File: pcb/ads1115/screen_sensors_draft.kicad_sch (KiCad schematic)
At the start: 12 parts, among them J1 WAVESHARE_I2C, J2 BOILER_PROBE, J3 XDB401_ANALOG, U1 ADS1115IDGSR, U2 SHT40-AD1B

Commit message: Screen Sensors PCB
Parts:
- J1: Note Pin 1 VCC/3V3, 2 GND, 3 SDA, 4 SCL; matches Waveshare order -> Pin 1 VCC/3V3, 2 GND, 3 SCL, 4 SDA; cross SDA/SCL in Wavesh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
- renumbered C4 to C3, C5 to C4, C6 to C5
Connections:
- net SCL: now also J1.3 (Pin_3); no longer J1.4 (Pin_4)
- net SDA: now also J1.4 (Pin_4); no longer J1.3 (Pin_3)
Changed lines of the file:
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@@
 (label "GND" (at 38.1 50.8 180) (effects (font (size 1.0 1.0))))
 (wire (pts (xy 43.18 53.34) (xy 38.1 53.34)) (stroke (width 0) (type default)))
-(label "SDA" (at 38.1 53.34 180) (effects (font (size 1.0 1.0))))
+(label "SCL" (at 38.1 53.34 180) (effects (font (size 1.0 1.0))))
 (wire (pts (xy 43.18 55.88) (xy 38.1 55.88)) (stroke (width 0) (type default)))
-(label "SCL" (at 38.1 55.88 180) (effects (font (size 1.0 1.0))))
+(label "SDA" (at 38.1 55.88 180) (effects (font (size 1.0 1.0))))
 (symbol (lib_id "Connector_Generic:Conn_01x04") (at 48.26 50.8 0) (unit 1) (in_bom yes) (on_board yes) (dnp no)
 (property "Reference" "J1" (at 48.26 45.72 0) (effects (font (size 1.0 1.0)) ))
@@
 (property "MPN" "B4B-XH-A(LF)(SN)" (at 48.26 58.8 0) (effects (font (size 1.0 1.0)) (hide yes)))
 (property "LCSC" "C144395" (at 48.26 58.8 0) (effects (font (size 1.0 1.0)) (hide yes)))
-(property "Note" "Pin 1 VCC/3V3, 2 GND, 3 SDA, 4 SCL; matches Waveshare order" (at 48.26 58.8 0) (effects (font (size 1.0 1.0)) (hide yes)))
+(property "Note" "Pin 1 VCC/3V3, 2 GND, 3 SCL, 4 SDA; cross SDA/SCL in Waveshare cable" (at 48.26 58.8 0) (effects (font (size 1.0 1.0)) (hide yes)))
 (pin "1")
 (pin "2")
@@
 (label "GND" (at 238.76 125.73 0) (effects (font (size 1.0 1.0))))
 (symbol (lib_id "Device:C") (at 233.68 116.84 0) (unit 1) (in_bom yes) (on_board yes) (dnp no)
-(property "Reference" "C4" (at 234.315 114.3 0) (effects (font (size 1.0 1.0)) ))
+(property "Reference" "C3" (at 234.315 114.3 0) (effects (font (size 1.0 1.0)) ))
 (property "Value" "100nF" (at 234.315 119.38000000000001 0) (effects (font (size 1.0 1.0)) ))
 (property "Footprint" "Capacitor_SMD:C_0603_1608Metric" (at 234.64520000000002 120.65 0) (effects (font (size 1.0 1.0)) (hide yes)))
@@
 (pin "1")
 (pin "2")
-(instances (project "screen_sensors_draft" (path "/b733619e-0a21-4de7-9d63-5b29c9c92157" (reference "C4") (unit 1)))) )
+(instances (project "screen_sensors_draft" (path "/b733619e-0a21-4de7-9d63-5b29c9c92157" (reference "C3") (unit 1)))) )
 (wire (pts (xy 259.08 113.03) (xy 259.08 107.95)) (stroke (width 0) (type default)))
 (wire (pts (xy 259.08 107.95) (xy 264.16 107.95)) (stroke (width 0) (type default)))
@@
 (label "GND" (at 264.16 125.73 0) (effects (font (size 1.0 1.0))))
 (symbol (lib_id "Device:C") (at 259.08 116.84 0) (unit 1) (in_bom yes) (on_board yes) (dnp no)
-(property "Reference" "C5" (at 259.715 114.3 0) (effects (font (size 1.0 1.0)) ))
+(property "Reference" "C4" (at 259.715 114.3 0) (effects (font (size 1.0 1.0)) ))
 (property "Value" "100nF" (at 259.715 119.38000000000001 0) (effects (font (size 1.0 1.0)) ))
 (property "Footprint" "Capacitor_SMD:C_0603_1608Metric" (at 260.04519999999997 120.65 0) (effects (font (size 1.0 1.0)) (hide yes)))
@@
 (pin "1")
 (pin "2")
-(instances (project "screen_sensors_draft" (path "/b733619e-0a21-4de7-9d63-5b29c9c92157" (reference "C5") (unit 1)))) )
+(instances (project "screen_sensors_draft" (path "/b733619e-0a21-4de7-9d63-5b29c9c92157" (reference "C4") (unit 1)))) )
 (text "No voltage divider / amplifier needed. Pressure = 6*(Vout-0.4) bar nominal." (at 155 135 0) (effects (font (size 1.1 1.1)) (justify left)))
 (text "Verify supply current, output impedance, startup and ratiometry before manufacture." (at 155 141 0) (effects (font (size 1.1 1.1)) (justify left)))
@@
 (label "GND" (at 88.9 184.15 0) (effects (font (size 1.0 1.0))))
 (symbol (lib_id "Device:C") (at 83.82 175.26 0) (unit 1) (in_bom yes) (on_board yes) (dnp no)
-(property "Reference" "C6" (at 84.455 172.72 0) (effects (font (size 1.0 1.0)) ))
+(property "Reference" "C5" (at 84.455 172.72 0) (effects (font (size 1.0 1.0)) ))
 (property "Value" "100nF" (at 84.455 177.79999999999998 0) (effects (font (size 1.0 1.0)) ))
 (property "Footprint" "Capacitor_SMD:C_0603_1608Metric" (at 84.78519999999999 179.07 0) (effects (font (size 1.0 1.0)) (hide yes)))
@@
 (pin "1")
 (pin "2")
-(instances (project "screen_sensors_draft" (path "/b733619e-0a21-4de7-9d63-5b29c9c92157" (reference "C6") (unit 1)))) )
+(instances (project "screen_sensors_draft" (path "/b733619e-0a21-4de7-9d63-5b29c9c92157" (reference "C5") (unit 1)))) )
 (text "Place near board edge, exposed to box air, away from display heat." (at 20 194 0) (effects (font (size 1.1 1.1)) (justify left)))
 (text "Humidity sensor opening must remain free of flux, coating and adhesives." (at 20 200 0) (effects (font (size 1.1 1.1)) (justify left)))

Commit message: pcb update
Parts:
- added D1: RED / POWER, LED_SMD:LED_0603_1608Metric, symbol Device:LED
- added R4: 2.2k, Resistor_SMD:R_0603_1608Metric, symbol Device:R
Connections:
- net 3V3: now also R4.1
- net GND: now also D1.1 (K)
- new net: D1.2 (A), R4.2
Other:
- note added: "POWER: 3V3 present; does not verify I2C communication."
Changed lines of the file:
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@@
 (text "Place near board edge, exposed to box air, away from display heat." (at 20 194 0) (effects (font (size 1.1 1.1)) (justify left)))
 (text "Humidity sensor opening must remain free of flux, coating and adhesives." (at 20 200 0) (effects (font (size 1.1 1.1)) (justify left)))
+(wire (pts (xy 120.65 44.45) (xy 120.65 39.37)) (stroke (width 0) (type default)))
+(wire (pts (xy 120.65 39.37) (xy 125.73 39.37)) (stroke (width 0) (type default)))
+(label "3V3" (at 125.73 39.37 0) (effects (font (size 1.0 1.0))))
+(wire (pts (xy 120.65 52.07) (xy 120.65 59.69)) (stroke (width 0) (type default)))
+(wire (pts (xy 120.65 67.31) (xy 120.65 72.39)) (stroke (width 0) (type default)))
+(wire (pts (xy 120.65 72.39) (xy 125.73 72.39)) (stroke (width 0) (type default)))
+(label "GND" (at 125.73 72.39 0) (effects (font (size 1.0 1.0))))
+(symbol (lib_id "Device:R") (at 120.65 48.26 0) (unit 1) (in_bom yes) (on_board yes) (dnp no)
+(property "Reference" "R4" (at 125.73 46.989999999999995 0) (effects (font (size 1.0 1.0)) (justify left)))
+(property "Value" "2.2k" (at 125.73 49.53 0) (effects (font (size 1.0 1.0)) (justify left)))
+(property "Footprint" "Resistor_SMD:R_0603_1608Metric" (at 120.65 48.26 0) (effects (font (size 1.0 1.0)) (hide yes)))
+(property "Datasheet" "" (at 120.65 48.26 0) (effects (font (size 1.0 1.0)) (hide yes)))
+(property "MPN" "0603WAF2201T5E" (at 120.65 48.26 0) (effects (font (size 1.0 1.0)) (hide yes)))
+(property "LCSC" "C4190" (at 120.65 48.26 0) (effects (font (size 1.0 1.0)) (hide yes)))
+(property "Note" "JLCPCB basic; 1%; power LED current limiting" (at 120.65 48.26 0) (effects (font (size 1.0 1.0)) (hide yes)))
+(pin "1")
+(pin "2")
+(instances (project "screen_sensors_draft" (path "/b733619e-0a21-4de7-9d63-5b29c9c92157" (reference "R4") (unit 1)))) )
+(symbol (lib_id "Device:LED") (at 120.65 63.5 90) (unit 1) (in_bom yes) (on_board yes) (dnp no)
+(property "Reference" "D1" (at 125.73 62.23 0) (effects (font (size 1.0 1.0)) (justify left)))
+(property "Value" "RED / POWER" (at 125.73 64.77 0) (effects (font (size 1.0 1.0)) (justify left)))
+(property "Footprint" "LED_SMD:LED_0603_1608Metric" (at 120.65 63.5 0) (effects (font (size 1.0 1.0)) (hide yes)))
+(property "Datasheet" "" (at 120.65 63.5 0) (effects (font (size 1.0 1.0)) (hide yes)))
+(property "MPN" "KT-0603R" (at 120.65 63.5 0) (effects (font (size 1.0 1.0)) (hide yes)))
+(property "LCSC" "C2286" (at 120.65 63.5 0) (effects (font (size 1.0 1.0)) (hide yes)))
+(property "Note" "JLCPCB basic; red power indicator; approximately 0.6mA; pin 1 cathode to GND" (at 120.65 63.5 0) (effects (font (size 1.0 1.0)) (hide yes)))
+(pin "1")
+(pin "2")
+(instances (project "screen_sensors_draft" (path "/b733619e-0a21-4de7-9d63-5b29c9c92157" (reference "D1") (unit 1)))) )
+(text "POWER: 3V3 present; does not verify I2C communication." (at 20 84 0) (effects (font (size 1.1 1.1)) (justify left)))
 (sheet_instances (path "/" (page "1"))) (embedded_fonts no))

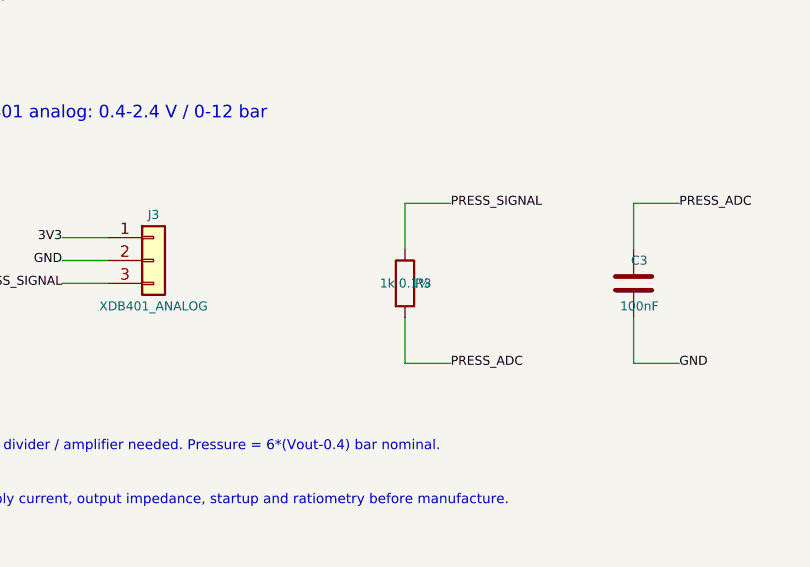
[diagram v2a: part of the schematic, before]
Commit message: Use basic pressure resistor and add JLCPCB manufacturing exporter
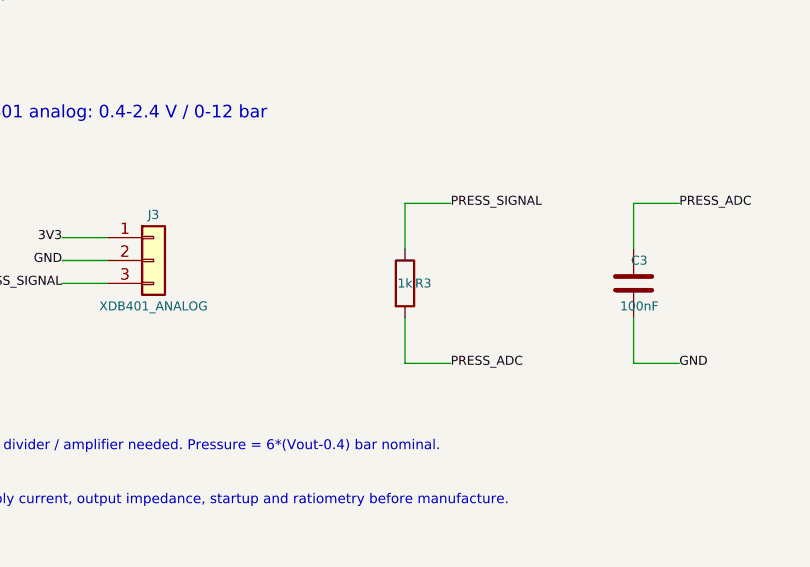
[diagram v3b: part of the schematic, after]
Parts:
- R3: value 1k 0.1% -> 1k; LCSC C394536 -> C21190; MPN PTFR0603B1K00N9 -> 0603WAF1001T5E
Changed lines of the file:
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@@
 (symbol (lib_id "Device:R") (at 208.28 116.84 0) (unit 1) (in_bom yes) (on_board yes) (dnp no)
 (property "Reference" "R3" (at 210.312 116.84 0) (effects (font (size 1.0 1.0)) ))
-(property "Value" "1k 0.1%" (at 208.28 116.84 0) (effects (font (size 1.0 1.0)) ))
+(property "Value" "1k" (at 208.28 116.84 0) (effects (font (size 1.0 1.0)) ))
 (property "Footprint" "Resistor_SMD:R_0603_1608Metric" (at 206.502 116.84 0) (effects (font (size 1.0 1.0)) (hide yes)))
 (property "Datasheet" "" (at 208.28 116.84 0) (effects (font (size 1.0 1.0)) (hide yes)))
 (property "Note" "Provisional RF filter; can assemble 0R instead" (at 208.28 124.84 0) (effects (font (size 1.0 1.0)) (hide yes)))
-(property "MPN" "PTFR0603B1K00N9" (at 208.28 124.84 0) (effects (font (size 1.0 1.0)) (hide yes)))
-(property "LCSC" "C394536" (at 208.28 124.84 0) (effects (font (size 1.0 1.0)) (hide yes)))
+(property "MPN" "0603WAF1001T5E" (at 208.28 124.84 0) (effects (font (size 1.0 1.0)) (hide yes)))
+(property "LCSC" "C21190" (at 208.28 124.84 0) (effects (font (size 1.0 1.0)) (hide yes)))
 (pin "1")
 (pin "2")
